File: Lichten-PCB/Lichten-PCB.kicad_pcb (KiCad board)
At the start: 2 copper layers, 51 parts, among them J1 Conn_01x04_Socket

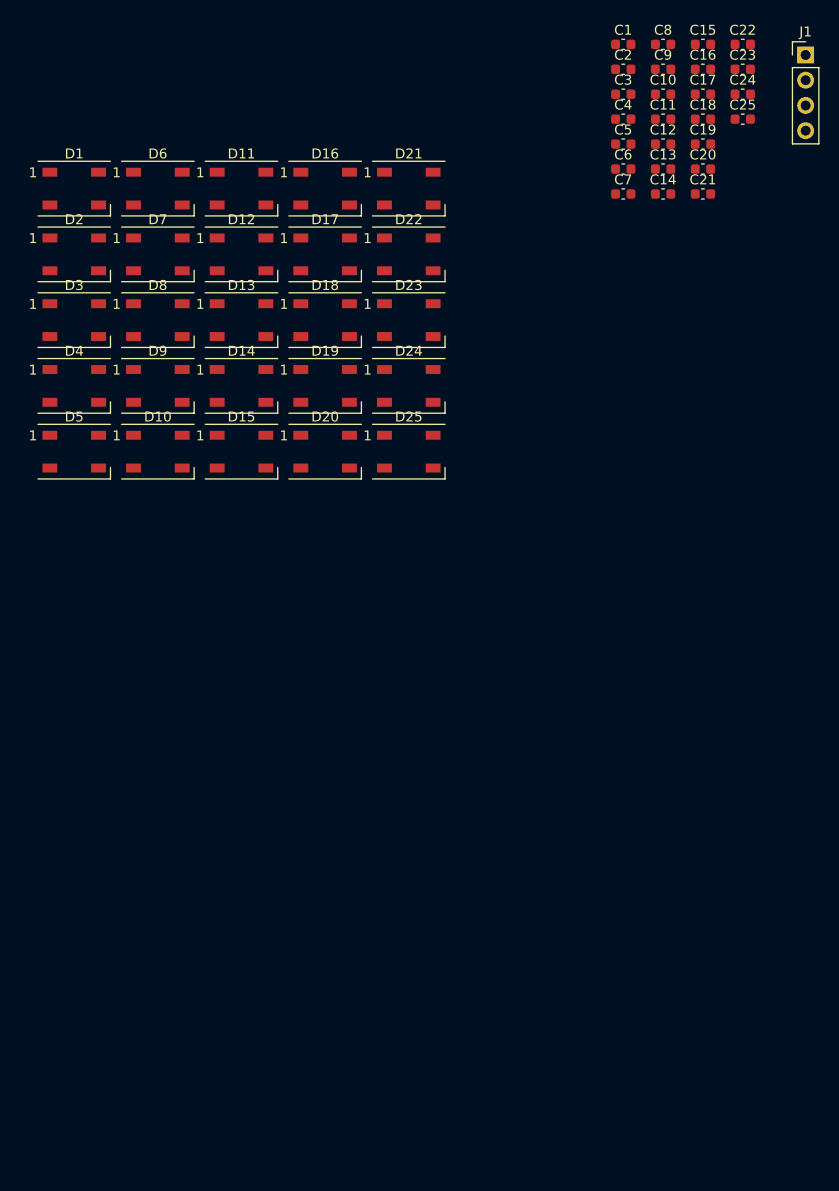
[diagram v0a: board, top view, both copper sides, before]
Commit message: Componenten geplaatst
Paar fouten opgelost namen juist gemaakt en niet gelinked connecties vastgemaakt.
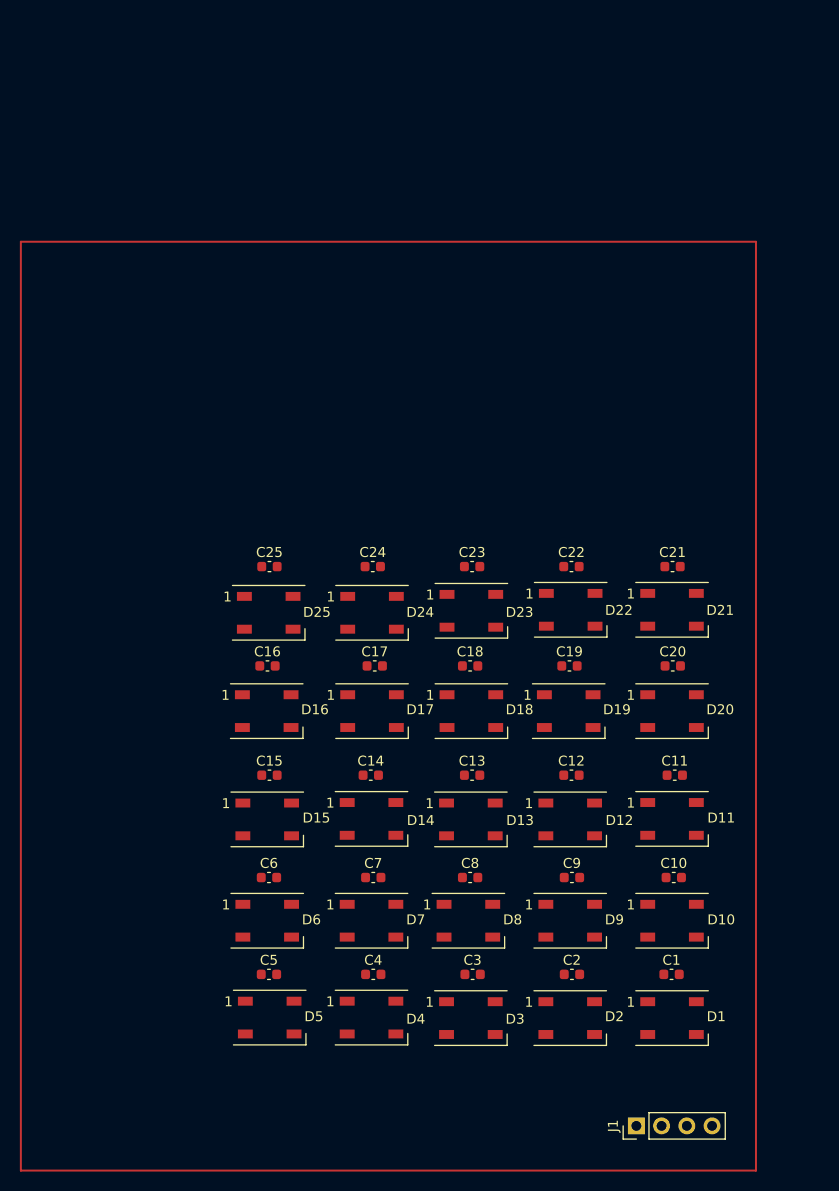
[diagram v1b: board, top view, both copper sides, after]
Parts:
- moved J1 109.1 mm to (162.0, 129.5), turned to 90 degrees
- moved D1 102.9 mm to (165.6, 118.7)
- moved C1 93.7 mm to (165.5, 114.2)
- moved D2 91.7 mm to (155.3, 118.7)
- moved C2 91.3 mm to (155.5, 114.2)
- moved C5 90.9 mm to (125.0, 114.2)
- moved C3 89.9 mm to (145.5, 114.2)
- moved C4 89.7 mm to (135.5, 114.2)
- moved C8 86.1 mm to (145.2, 104.5)
- moved C15 85.5 mm to (125.0, 94.2)
- moved C9 81.9 mm to (155.5, 104.5)
- moved D3 80.8 mm to (145.3, 118.7)
- moved C6 79.7 mm to (125.0, 104.5)
- moved C10 78.9 mm to (165.7, 104.5)
- moved D11 76.8 mm to (165.6, 98.6)
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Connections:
- D10 pad 4: unconnected-(D10-DIN-Pad4) -> Net-(D10-DIN)
- D9 pad 2: unconnected-(D9-DOUT-Pad2) -> Net-(D10-DIN)
- J1 pad 1: 3V3 -> +3V3

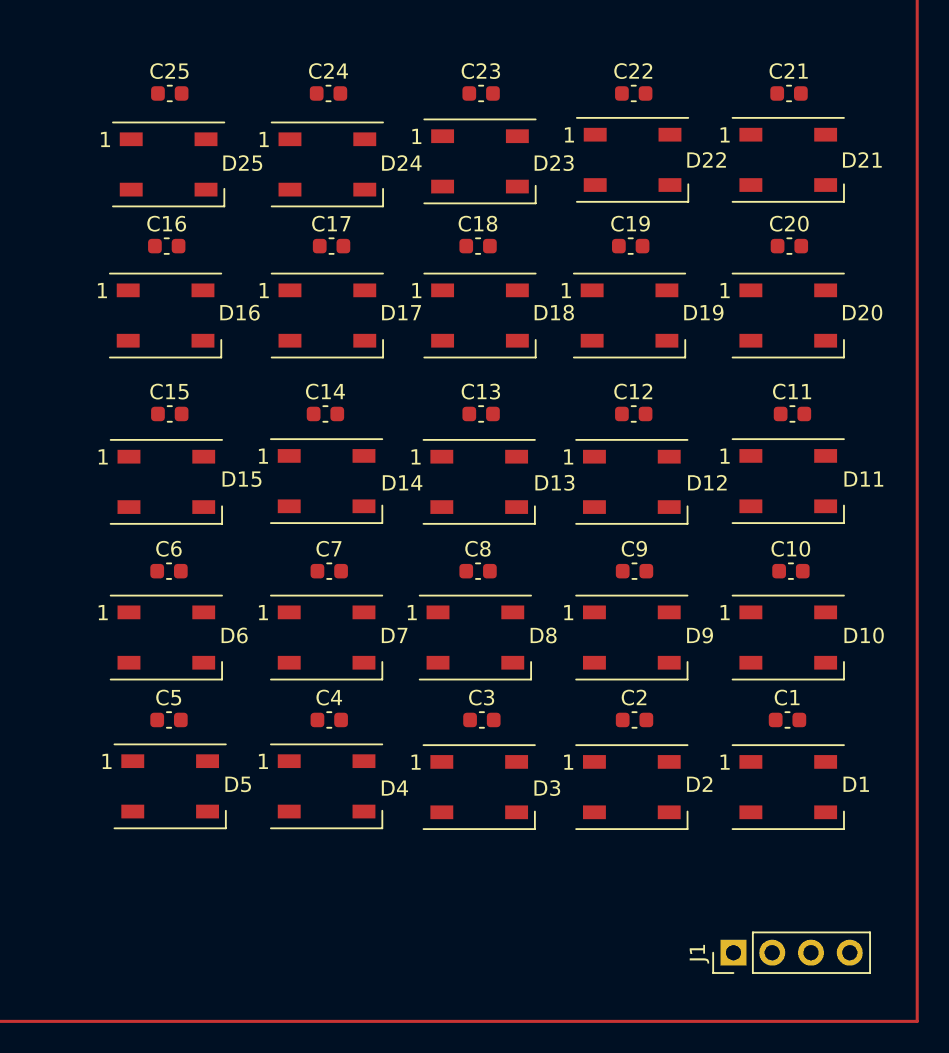
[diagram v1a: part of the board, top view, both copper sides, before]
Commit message: Bekabeling van de power en data
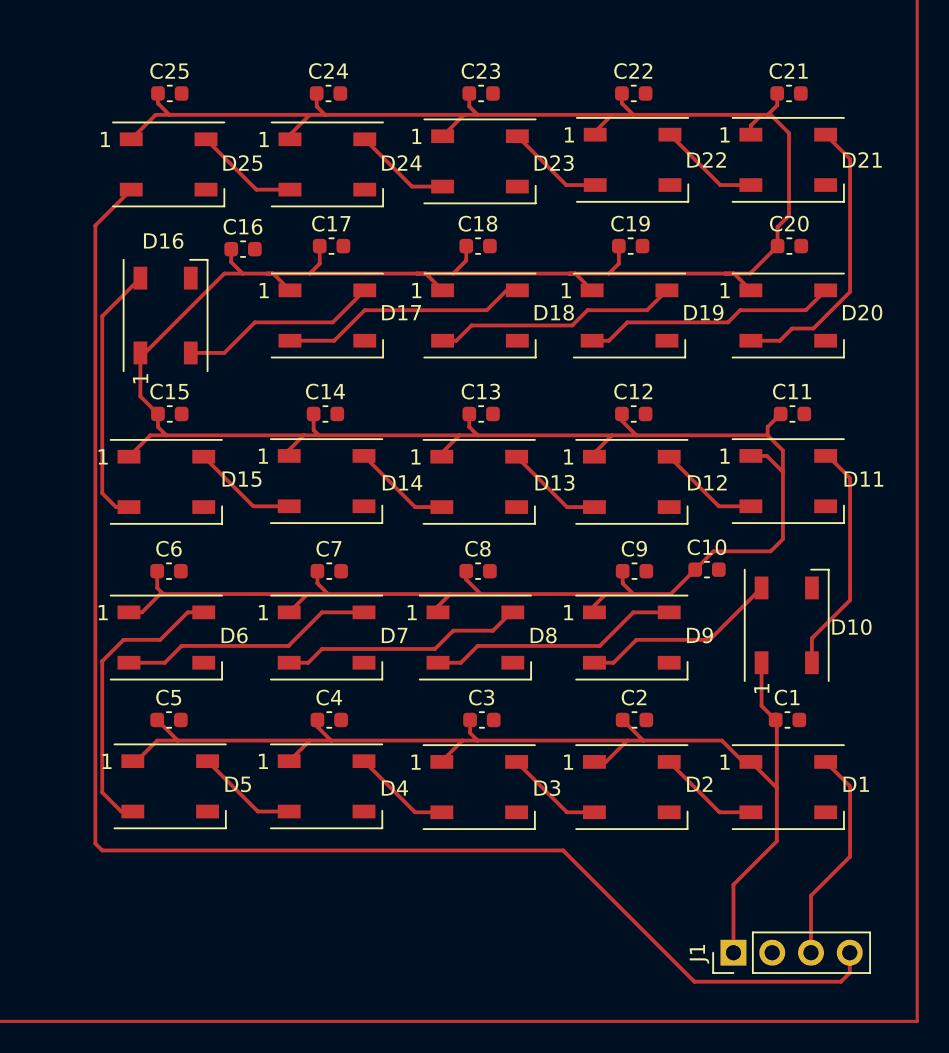
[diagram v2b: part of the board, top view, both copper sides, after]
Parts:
- moved C10 5.50 mm to (160.2, 104.4)
- moved C16 5.00 mm to (129.8, 83.4)
- moved D10 0.81 mm to (165.4, 108.0), turned to 90 degrees
- turned D16 to 90 degrees
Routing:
- net +3V3: track 0.00 -> 335.2 mm
- net DOUT: track 0.00 -> 98.6 mm
- net Net-(D5-DOUT): track 0.00 -> 19.1 mm
- net Net-(D20-DOUT): track 0.00 -> 18.8 mm
- net Net-(D15-DOUT): track 0.00 -> 17.3 mm
- net Net-(D6-DOUT): track 0.00 -> 16.8 mm
- net Net-(D19-DOUT): track 0.00 -> 16.7 mm
- net Net-(D8-DOUT): track 0.00 -> 16.5 mm
- net Net-(D17-DOUT): track 0.00 -> 16.3 mm
- net Net-(D18-DOUT): track 0.00 -> 16.1 mm
- net Net-(D7-DOUT): track 0.00 -> 16.0 mm
- net Net-(D10-DOUT): track 0.00 -> 15.3 mm
- net DIN: track 0.00 -> 14.2 mm
- net Net-(D16-DOUT): track 0.00 -> 13.1 mm
- net Net-(D10-DIN): track 0.00 -> 13.0 mm
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
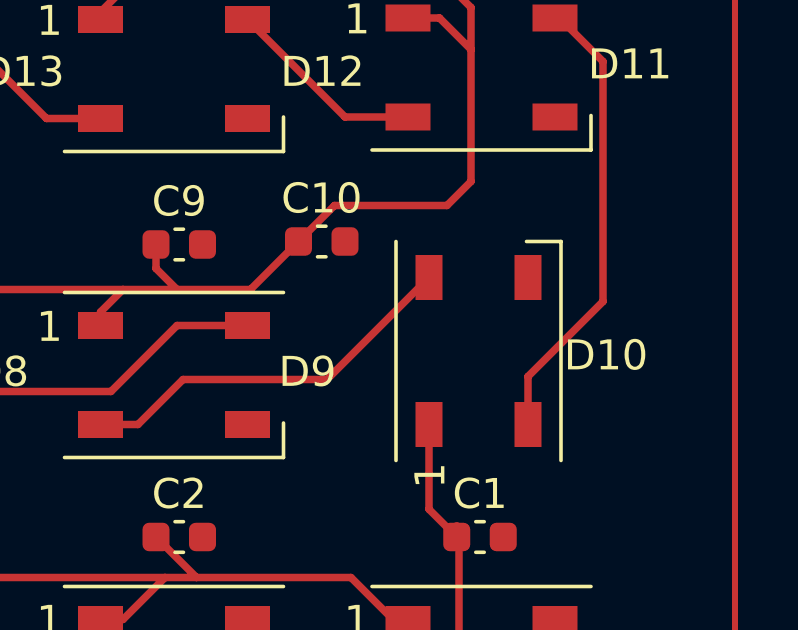
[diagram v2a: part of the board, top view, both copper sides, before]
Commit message: alle 3V3 geconnect
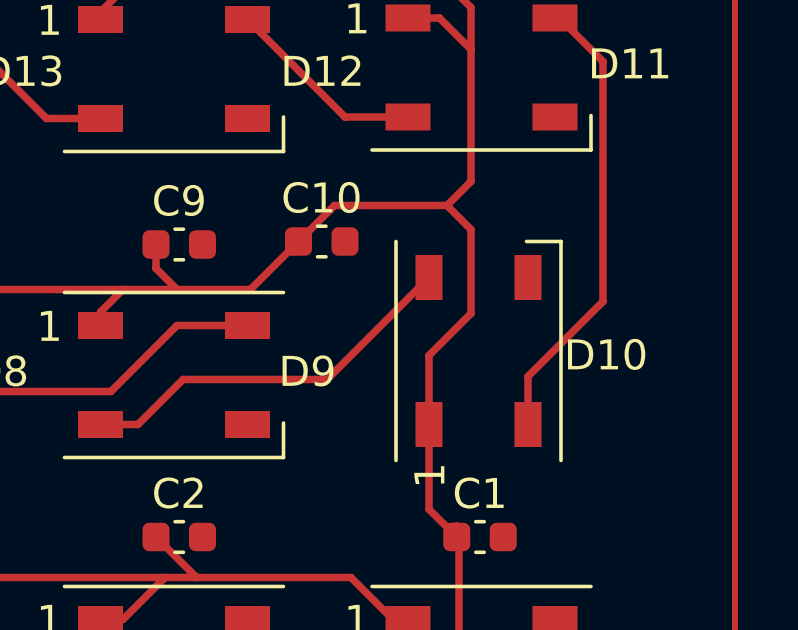
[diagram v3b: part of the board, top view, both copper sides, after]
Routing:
- net +3V3: track 335.2 -> 343.4 mm
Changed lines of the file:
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@@
   (segment (start 144.7 114.25) (end 144.7 115.1) (width 0.25) (layer "F.Cu") (net 1))
   (segment (start 164.4 74.6) (end 164.2 74.6) (width 0.25) (layer "F.Cu") (net 1))
+  (segment (start 163.8 108.2) (end 165.2 106.8) (width 0.25) (layer "F.Cu") (net 1))
   (segment (start 142.85 117) (end 142.85 116.95) (width 0.25) (layer "F.Cu") (net 1))
   (segment (start 125 74.6) (end 124.25 73.85) (width 0.25) (layer "F.Cu") (net 1))
@@
   (segment (start 164.15 96.95) (end 163.1 96.95) (width 0.25) (layer "F.Cu") (net 1))
   (segment (start 134.45 95.25) (end 134.8 95.6) (width 0.25) (layer "F.Cu") (net 1))
+  (segment (start 163.8 110.5) (end 163.8 108.2) (width 0.25) (layer "F.Cu") (net 1))
   (segment (start 144.2 115.6) (end 135.6 115.6) (width 0.25) (layer "F.Cu") (net 1))
   (segment (start 163.1 75.3) (end 163.1 75.9) (width 0.25) (layer "F.Cu") (net 1))
@@
   (segment (start 123.75 95.6) (end 122.35 97) (width 0.25) (layer "F.Cu") (net 1))
   (segment (start 144.45 84.15) (end 143.6 85) (width 0.25) (layer "F.Cu") (net 1))
+  (segment (start 165.2 106.8) (end 165.2 104) (width 0.25) (layer "F.Cu") (net 1))
   (segment (start 165.2 98) (end 164.15 96.95) (width 0.25) (layer "F.Cu") (net 1))
   (segment (start 165.6 81.2) (end 165.6 75.8) (width 0.25) (layer "F.Cu") (net 1))
@@
   (segment (start 156.05 115.6) (end 155 115.6) (width 0.25) (layer "F.Cu") (net 1))
   (segment (start 151.2 85) (end 153.8 85) (width 0.25) (layer "F.Cu") (net 1))
+  (segment (start 165.2 104) (end 164.4 103.2) (width 0.25) (layer "F.Cu") (net 1))
   (segment (start 129.8 85) (end 129.05 84.25) (width 0.25) (layer "F.Cu") (net 1))
   (segment (start 125.55 115.6) (end 124.2 115.6) (width 0.25) (layer "F.Cu") (net 1))

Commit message: ground plane toegevoegd
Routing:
- net DOUT: track 98.6 -> 97.4 mm
- added copper zone on B.Cu, net GND
- added copper zone on F.Cu, net GND
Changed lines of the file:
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@@
     )
   )
+  (gr_line (start 118.2 132.2) (end 118.2 69.8)
+    (stroke (width 0.2) (type default)) (layer "F.Cu"))
   (gr_line (start 100 134) (end 174 134)
     (stroke (width 0.2) (type default)) (layer "F.Cu"))
   (gr_line (start 174 134) (end 174 40.5)
     (stroke (width 0.2) (type default)) (layer "F.Cu"))
+  (gr_line (start 118.2 69.8) (end 172.4 70)
+    (stroke (width 0.2) (type default)) (layer "F.Cu"))
   (gr_line (start 174 40.5) (end 100 40.5)
     (stroke (width 0.2) (type default)) (layer "F.Cu"))
+  (gr_line (start 172 132) (end 172 132.2)
+    (stroke (width 0.2) (type default)) (layer "F.Cu"))
+  (gr_line (start 172 132.2) (end 171.4 132.2)
+    (stroke (width 0.2) (type default)) (layer "F.Cu"))
   (gr_line (start 100 40.5) (end 100 134)
     (stroke (width 0.2) (type default)) (layer "F.Cu"))
+  (gr_line (start 171.4 132.2) (end 118.2 132.2)
+    (stroke (width 0.2) (type default)) (layer "F.Cu"))
+  (gr_line (start 172.4 70) (end 172 132)
+    (stroke (width 0.2) (type default)) (layer "F.Cu"))
+  (segment (start 165 103.8) (end 164.4 103.2) (width 0.25) (layer "F.Cu") (net 1))
   (segment (start 134.2 74.6) (end 132.9 75.9) (width 0.25) (layer "F.Cu") (net 1))
   (segment (start 144.7 115.1) (end 145.2 115.6) (width 0.25) (layer "F.Cu") (net 1))
@@
   (segment (start 144.7 114.25) (end 144.7 115.1) (width 0.25) (layer "F.Cu") (net 1))
   (segment (start 164.4 74.6) (end 164.2 74.6) (width 0.25) (layer "F.Cu") (net 1))
-  (segment (start 163.8 108.2) (end 165.2 106.8) (width 0.25) (layer "F.Cu") (net 1))
   (segment (start 142.85 117) (end 142.85 116.95) (width 0.25) (layer "F.Cu") (net 1))
   (segment (start 125 74.6) (end 124.25 73.85) (width 0.25) (layer "F.Cu") (net 1))
@@
   (segment (start 154 95.6) (end 145.2 95.6) (width 0.25) (layer "F.Cu") (net 1))
   (segment (start 162.6 117) (end 161.2 115.6) (width 0.25) (layer "F.Cu") (net 1))
+  (segment (start 165 107.4) (end 165 103.8) (width 0.25) (layer "F.Cu") (net 1))
   (segment (start 164.15 96.95) (end 163.1 96.95) (width 0.25) (layer "F.Cu") (net 1))
   (segment (start 134.45 95.25) (end 134.8 95.6) (width 0.25) (layer "F.Cu") (net 1))
-  (segment (start 163.8 110.5) (end 163.8 108.2) (width 0.25) (layer "F.Cu") (net 1))
   (segment (start 144.2 115.6) (end 135.6 115.6) (width 0.25) (layer "F.Cu") (net 1))
   (segment (start 163.1 75.3) (end 163.1 75.9) (width 0.25) (layer "F.Cu") (net 1))
@@
   (segment (start 125.55 115.6) (end 124.2 114.25) (width 0.25) (layer "F.Cu") (net 1))
   (segment (start 161.96 129.5) (end 161.96 125.04) (width 0.25) (layer "F.Cu") (net 1))
+  (segment (start 163.8 108.6) (end 165 107.4) (width 0.25) (layer "F.Cu") (net 1))
   (segment (start 124.6 106) (end 124.2 105.6) (width 0.25) (layer "F.Cu") (net 1))
   (segment (start 164.2 74.6) (end 163.8 74.6) (width 0.25) (layer "F.Cu") (net 1))
@@
   (segment (start 165.6 75.8) (end 164.4 74.6) (width 0.25) (layer "F.Cu") (net 1))
   (segment (start 164.8 118.7) (end 163.1 117) (width 0.25) (layer "F.Cu") (net 1))
+  (segment (start 163.8 110.5) (end 163.8 108.6) (width 0.25) (layer "F.Cu") (net 1))
   (segment (start 129.05 84.25) (end 129.05 83.4) (width 0.25) (layer "F.Cu") (net 1))
   (segment (start 123.4 90.2) (end 128.6 85) (width 0.25) (layer "F.Cu") (net 1))
@@
   (segment (start 123.75 95.6) (end 122.35 97) (width 0.25) (layer "F.Cu") (net 1))
   (segment (start 144.45 84.15) (end 143.6 85) (width 0.25) (layer "F.Cu") (net 1))
-  (segment (start 165.2 106.8) (end 165.2 104) (width 0.25) (layer "F.Cu") (net 1))
   (segment (start 165.2 98) (end 164.15 96.95) (width 0.25) (layer "F.Cu") (net 1))
   (segment (start 165.6 81.2) (end 165.6 75.8) (width 0.25) (layer "F.Cu") (net 1))
@@
   (segment (start 156.05 115.6) (end 155 115.6) (width 0.25) (layer "F.Cu") (net 1))
   (segment (start 151.2 85) (end 153.8 85) (width 0.25) (layer "F.Cu") (net 1))
-  (segment (start 165.2 104) (end 164.4 103.2) (width 0.25) (layer "F.Cu") (net 1))
   (segment (start 129.8 85) (end 129.05 84.25) (width 0.25) (layer "F.Cu") (net 1))
   (segment (start 125.55 115.6) (end 124.2 115.6) (width 0.25) (layer "F.Cu") (net 1))
@@
   (segment (start 132.9 79.5) (end 130.7 79.5) (width 0.25) (layer "F.Cu") (net 26))
   (segment (start 169.58 130.82) (end 169.58 129.5) (width 0.25) (layer "F.Cu") (net 27))
-  (segment (start 150.8 122.8) (end 159.4 131.4) (width 0.25) (layer "F.Cu") (net 27))
-  (segment (start 120.6 122.8) (end 150.8 122.8) (width 0.25) (layer "F.Cu") (net 27))
-  (segment (start 120.15 122.35) (end 120.6 122.8) (width 0.25) (layer "F.Cu") (net 27))
+  (segment (start 120 120) (end 128.4 128.4) (width 0.25) (layer "F.Cu") (net 27))
+  (segment (start 156.4 128.4) (end 159.4 131.4) (width 0.25) (layer "F.Cu") (net 27))
+  (segment (start 122.5 79.5) (end 120 82) (width 0.25) (layer "F.Cu") (net 27))
+  (segment (start 120 82) (end 120 120) (width 0.25) (layer "F.Cu") (net 27))
+  (segment (start 128.4 128.4) (end 156.4 128.4) (width 0.25) (layer "F.Cu") (net 27))
+  (segment (start 169 131.4) (end 169.58 130.82) (width 0.25) (layer "F.Cu") (net 27))
   (segment (start 159.4 131.4) (end 169 131.4) (width 0.25) (layer "F.Cu") (net 27))
-  (segment (start 122.5 79.5) (end 120.15 81.85) (width 0.25) (layer "F.Cu") (net 27))
-  (segment (start 120.15 81.85) (end 120.15 122.35) (width 0.25) (layer "F.Cu") (net 27))
-  (segment (start 169 131.4) (end 169.58 130.82) (width 0.25) (layer "F.Cu") (net 27))
   (segment (start 154.1 110.5) (end 155.6 109) (width 0.25) (layer "F.Cu") (net 28))
   (segment (start 152.85 110.5) (end 154.1 110.5) (width 0.25) (layer "F.Cu") (net 28))
   (segment (start 160.4 109) (end 163.8 105.6) (width 0.25) (layer "F.Cu") (net 28))
   (segment (start 155.6 109) (end 160.4 109) (width 0.25) (layer "F.Cu") (net 28))
+  (zone (net 3) (net_name "GND") (layers "F&B.Cu") (hatch edge 0.5)
+    (connect_pads (clearance 0.5))
+    (min_thickness 0.25) (filled_areas_thickness no)
+    (fill yes (thermal_gap 0.5) (thermal_bridge_width 0.5))
+    (polygon
+      (pts
+        (xy 118.2 69.8)
+        (xy 118.2 132.2)
+        (xy 172 132.2)
+        (xy 172.4 70)
+      )
+    )
+  )
 )

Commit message: Via geplaatst en beetje verbeterd
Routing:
- net +3V3: track 343.2 -> 342.2 mm
- net GND: vias 0 -> 16

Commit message: Edge cuts en via toegevoegd met wat silk screen
Misschien op de achterkant een leuke foto van een aap
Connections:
- net Net-(D1-DOUT) renamed /LED's/Data-1
- net Net-(D10-DIN) renamed /LED's/Data-9
- net Net-(D10-DOUT) renamed /LED's/Data-10
- net Net-(D11-DOUT) renamed /LED's/Data-11
- net Net-(D12-DOUT) renamed /LED's/Data-12
- net Net-(D13-DOUT) renamed /LED's/Data-13
- net Net-(D15-DOUT) renamed /LED's/Data-15
- net Net-(D16-DOUT) renamed /LED's/Data-16
- net Net-(D17-DOUT) renamed /LED's/Data-17
- net Net-(D18-DOUT) renamed /LED's/Data-18
- net Net-(D19-DOUT) renamed /LED's/Data-19
- net Net-(D2-DOUT) renamed /LED's/Data-2
- net Net-(D20-DOUT) renamed /LED's/Data-20
- net Net-(D21-DOUT) renamed /LED's/Data-21
- net Net-(D22-DOUT) renamed /LED's/Data-22
- net Net-(D23-DOUT) renamed /LED's/Data-23
- net Net-(D24-DOUT) renamed /LED's/Data-24
- net Net-(D3-DOUT) renamed /LED's/Data-3
- net Net-(D4-DOUT) renamed /LED's/Data-4
- net Net-(D5-DOUT) renamed /LED's/Data-5
- net Net-(D6-DOUT) renamed /LED's/Data-6
- net Net-(D7-DOUT) renamed /LED's/Data-7
- net Net-(D8-DOUT) renamed /LED's/Data-8
- J1 pad 2: GND -> DOUT
- J1 pad 4: DOUT -> GND
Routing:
- net DOUT: track 97.4 -> 92.2 mm
- net +3V3: track 342.2 -> 341.5 mm
- net GND: vias 16 -> 91
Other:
- board outline added: 54.2 x 62.2 mm
- board text added: "+3V3 DOUT DIN GND"
- board text added: "A.Benaissa N.Ganga"
- board text added: "GOD SAID AND THERE IS LIGHGT"

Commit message: Foto toegevoegd
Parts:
- added G***: LOGO, LOGO, B.Cu at (145.3, 98.7)
